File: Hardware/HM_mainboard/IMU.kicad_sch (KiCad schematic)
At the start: 13 parts, among them U5 MC6470, U6 BNO055

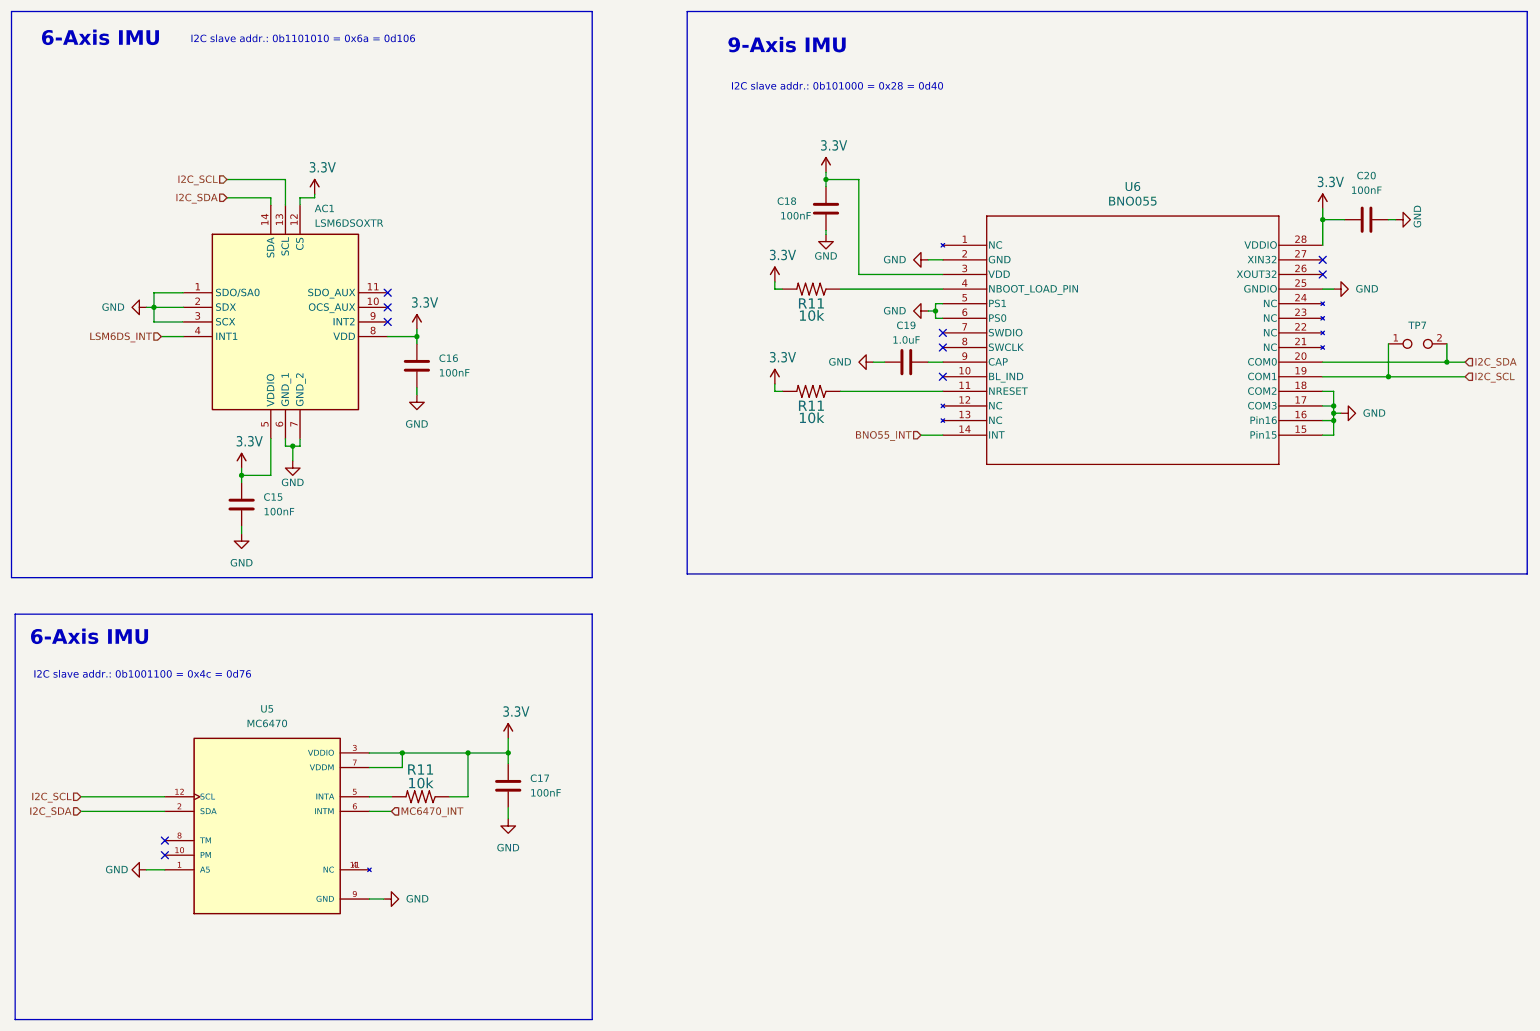
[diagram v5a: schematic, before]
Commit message: Updated schematic to version v2.0.0
•	Removed two 6-Axis IMUs
•	As the BNO055 did not respond to I2C requests, a 2k7 pullup was added in parallel to the I2C-SDA pullup. The behavior is described here:  https://forums.adafruit.com/viewtopic.php?t=205215
•	Added mounting holes for enclosure
•	Added board description prints
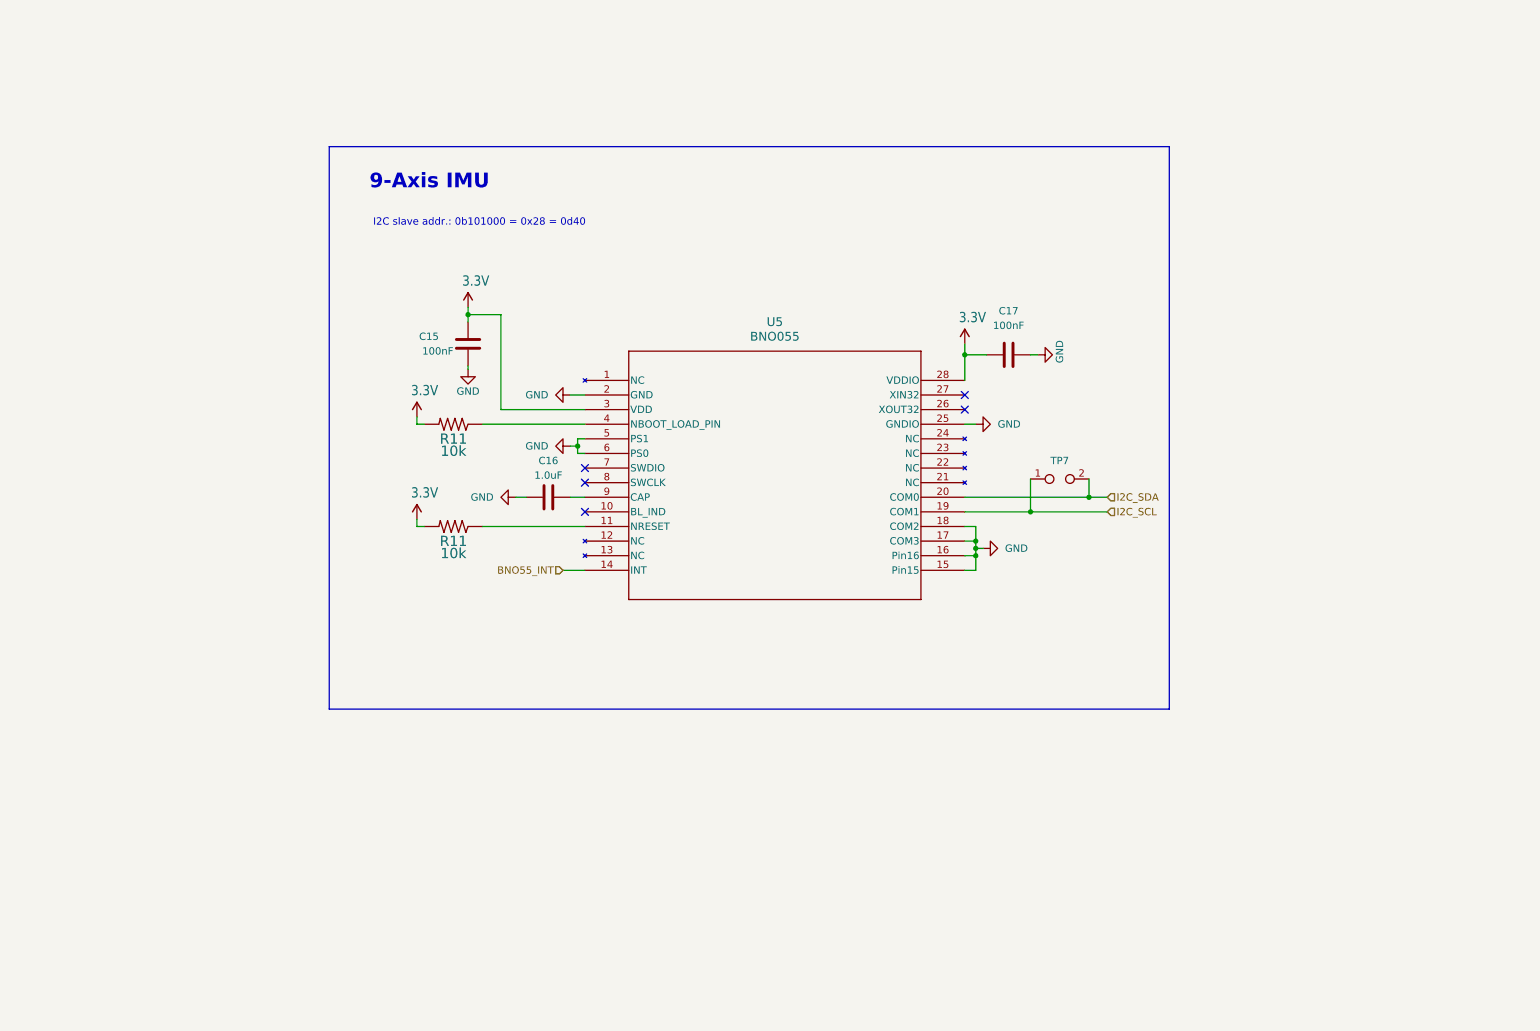
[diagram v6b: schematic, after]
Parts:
- removed AC1: LSM6DSOXTR, HeadMouse:LSM6DSOXTR, symbol LSM6DSOXTR:LSM6DSOXTR
- removed C15, C16, C17: 100nF, Capacitor_SMD:C_0603_1608Metric_Pad1.08x0.95mm_HandSolder, symbol Device:C
- removed R11: 10k, Resistor_SMD:R_0603_1608Metric_Pad0.98x0.95mm_HandSolder, symbol esp32-thing-eagle-import:10KOHM-1/10W-1%(0603)0603
- removed U5: MC6470, HeadMouse:PQFN50P200X200X100-12N, symbol HeadMouse:MC6470
- renumbered C18 to C15, C19 to C16, C20 to C17, U6 to U5
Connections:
- no-connect marks 10 -> 5
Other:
- note removed: "6-Axis IMU"
- note removed: "I2C slave addr.: 0b1001100 = 0x4c = 0d76"
- note removed: "I2C slave addr.: 0b1101010 = 0x6a = 0d106"
- moved on the sheet: C15, C16, C17, R11, TP7, U5

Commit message: Added BOM, PDF and zipped V2.0.0 project data
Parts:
- removed TP7: TestPoint_2Pole, Connector_PinHeader_2.54mm:PinHeader_1x02_P2.54mm_Vertical, symbol Connector:TestPoint_2Pole
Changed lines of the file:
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@@
     (title "Intertia_Measurement_Unit")
-  )
-  (junction (at 193.675 103.505) (diameter 0) (color 0 0 0 0)
-  )
-  (junction (at 203.835 100.965) (diameter 0) (color 0 0 0 0)
   )
   (junction (at 184.15 108.585) (diameter 0) (color 0 0 0 0)
@@
   (no_connect (at 182.245 83.185))
   (no_connect (at 116.205 95.885))
-  (wire (pts (xy 193.675 97.79) (xy 193.675 103.505))
-    (stroke (width 0) (type default))
-  )
   (wire (pts (xy 114.935 92.075) (xy 114.935 90.805))
     (stroke (width 0) (type default))
@@
     (stroke (width 0) (type default))
   )
-  (wire (pts (xy 203.835 100.965) (xy 207.01 100.965))
-    (stroke (width 0) (type default))
-  )
-  (wire (pts (xy 203.835 97.79) (xy 203.835 100.965))
+  (wire (pts (xy 182.245 100.965) (xy 185.42 100.965))
     (stroke (width 0) (type default))
   )
@@
     (stroke (width 0) (type default))
   )
-  (wire (pts (xy 193.675 103.505) (xy 207.01 103.505))
-    (stroke (width 0) (type default))
-  )
   (wire (pts (xy 185.42 109.855) (xy 184.15 109.855))
     (stroke (width 0) (type default))
   )
-  (wire (pts (xy 182.245 103.505) (xy 193.675 103.505))
+  (wire (pts (xy 182.245 103.505) (xy 185.42 103.505))
     (stroke (width 0) (type default))
   )
@@
   )
   (wire (pts (xy 182.245 108.585) (xy 184.15 108.585))
-    (stroke (width 0) (type default))
-  )
-  (wire (pts (xy 182.245 100.965) (xy 203.835 100.965))
     (stroke (width 0) (type default))
   )
@@
     (effects (font (size 1.27 1.27)) (justify right))
   )
-  (hierarchical_label "I2C_SCL" (shape input) (at 207.01 103.505 0) (fields_autoplaced)
+  (hierarchical_label "I2C_SCL" (shape input) (at 185.42 103.505 0) (fields_autoplaced)
     (effects (font (size 1.27 1.27)) (justify left))
   )
-  (hierarchical_label "I2C_SDA" (shape input) (at 207.01 100.965 0) (fields_autoplaced)
+  (hierarchical_label "I2C_SDA" (shape input) (at 185.42 100.965 0) (fields_autoplaced)
     (effects (font (size 1.27 1.27)) (justify left))
   )
@@
         )
       )
-    )
-  )
-  (symbol (lib_id "Connector:TestPoint_2Pole") (at 198.755 97.79 0) (unit 1)
-    (in_bom yes) (on_board yes) (dnp no) (fields_autoplaced)
-    (property "Reference" "TP7" (at 198.755 94.615 0)
-      (effects (font (size 1.27 1.27)))
-    )
-    (property "Value" "TestPoint_2Pole" (at 198.755 94.615 0)
-      (effects (font (size 1.27 1.27)) hide)
-    )
-    (property "Footprint" "Connector_PinHeader_2.54mm:PinHeader_1x02_P2.54mm_Vertical" (at 198.755 97.79 0)
-      (effects (font (size 1.27 1.27)) hide)
-    )
-    (property "Datasheet" "~" (at 198.755 97.79 0)
-      (effects (font (size 1.27 1.27)) hide)
-    )
-    (pin "1")
-    (pin "2")
-    (instances
-      (project "HM_mainboard"
-        (path "/54a6df43-5475-46a2-9916-8b0260700d4c/9043a365-e24a-41b8-9f6d-decb4da0da6a"
-          (reference "TP7") (unit 1)
-        )
-      )
